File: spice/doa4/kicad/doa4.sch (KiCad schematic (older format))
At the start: 15 parts, among them Q1 BC557, Q2 BC557, Q3 BC547, Q4 BC547, Q5 BC557, Q6 BC547, Q7 BC547

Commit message: schema doa4 cont.
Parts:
- added D5, D6, D7, D8: D1418, ~, symbol DIODE
- added Q10: BC547, TO92, symbol BC547
- added Q11: BD139, TO126, symbol BD139
- added Q12: BD140, TO126, symbol BD140
- added Q8, Q9: BC557, TO92, symbol BC557
- added RCS2, RE1: 150, ~, symbol R
- added RE2, RE3: 10, ~, symbol R
- added RSZ3: 3800, ~, symbol R
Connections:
- net labels added: Odiff, Out, VrefCS
- wire segments 14 -> 37
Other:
- moved on the sheet: D1, D2, D3, D4, Q1, Q2, Q3, Q4, Q5, Q6, Q7, RCS1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

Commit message: schema doa4 cont.
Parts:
- added Cp1: 10p, ~, symbol C
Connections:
- wire segments 37 -> 38
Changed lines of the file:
@@
 Connection ~ 7150 3500
 Connection ~ 7750 3600
+$Comp
+L C Cp1
+U 1 1 592DCC26
+P 5750 4000
+F 0 "Cp1" H 5750 4100 40  0000 L CNN
+F 1 "10p" H 5756 3915 40  0000 L CNN
+F 2 "~" H 5788 3850 30  0000 C CNN
+F 3 "~" H 5750 4000 60  0000 C CNN
+	1    5750 4000
+	-1   0    0    1
+$EndComp
+Wire Wire Line
+	6000 3800 5750 3800
 $EndSCHEMATC

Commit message: doa4 cont
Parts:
- added C4, C5: 0.1u, ~, symbol C
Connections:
- net labels added: GND
- wire segments 38 -> 41
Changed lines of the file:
@@
 Sheet 1 1
 Title ""
-Date "30 may 2017"
+Date "2 jun 2017"
 Rev ""
 Comp ""
@@
 	4100 2100 4100 2000
 Wire Wire Line
-	4100 2000 7250 2000
+	4100 2000 8400 2000
 Text Label 4250 2000 0    60   ~ 0
 V+
@@
 Connection ~ 4350 3900
 Wire Wire Line
-	3800 4900 7250 4900
+	3800 4900 8400 4900
 Text Label 4300 4300 0    60   ~ 0
 V-
@@
 Wire Wire Line
 	6000 3800 5750 3800
+$Comp
+L C C4
+U 1 1 59318096
+P 8400 2200
+F 0 "C4" H 8400 2300 40  0000 L CNN
+F 1 "0.1u" H 8406 2115 40  0000 L CNN
+F 2 "~" H 8438 2050 30  0000 C CNN
+F 3 "~" H 8400 2200 60  0000 C CNN
+	1    8400 2200
+	1    0    0    -1
+$EndComp
+$Comp
+L C C5
+U 1 1 593180A3
+P 8400 4700
+F 0 "C5" H 8400 4800 40  0000 L CNN
+F 1 "0.1u" H 8406 4615 40  0000 L CNN
+F 2 "~" H 8438 4550 30  0000 C CNN
+F 3 "~" H 8400 4700 60  0000 C CNN
+	1    8400 4700
+	1    0    0    -1
+$EndComp
+Connection ~ 7250 2000
+Connection ~ 7250 4900
+Wire Wire Line
+	8400 4500 8400 2400
+$Comp
+L GND #PWR01
+U 1 1 593181CB
+P 8750 3550
+F 0 "#PWR01" H 8750 3550 30  0001 C CNN
+F 1 "GND" H 8750 3480 30  0001 C CNN
+F 2 "" H 8750 3550 60  0000 C CNN
+F 3 "" H 8750 3550 60  0000 C CNN
+	1    8750 3550
+	1    0    0    -1
+$EndComp
+Wire Wire Line
+	8750 3550 8750 3400
+Wire Wire Line
+	8750 3400 8400 3400
+Connection ~ 8400 3400
+$Comp
+L PWR_FLAG #FLG02
+U 1 1 5931836C
+P 8400 4150
+F 0 "#FLG02" H 8400 4245 30  0001 C CNN
+F 1 "PWR_FLAG" H 8400 4330 30  0000 C CNN
+F 2 "" H 8400 4150 60  0000 C CNN
+F 3 "" H 8400 4150 60  0000 C CNN
+	1    8400 4150
+	0    1    1    0
+$EndComp
+Connection ~ 8400 4150
 $EndSCHEMATC

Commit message: doa4 kicad 4.05
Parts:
- C4, C5, Cp1: footprint ~ -> Doa4FPLibrary:C_Rect_L4.6mm_W3.0mm_P2.50mm_MKS02_FKP02_Doa4; symbol C -> C-RESCUE-doa4
- D1: footprint ~ -> Diodes_THT:D_DO-41_SOD81_P2.54mm_Vertical_AnodeUp
- D2: footprint ~ -> Doa4FPLibrary:D_DO-41_SOD81_P2.54mm_Vertical_AnodeUp_Doa4
- D3: value D14148 -> D1N4148; footprint ~ -> Doa4FPLibrary:D_DO-41_SOD81_P2.54mm_Vertical_AnodeUp_Doa4
- D4: value D1418 -> D1N4148; footprint ~ -> Doa4FPLibrary:D_DO-41_SOD81_P2.54mm_Vertical_AnodeUp_Doa4
- D5, D6, D7, D8: value D1418 -> D1N4148; footprint ~ -> (none)
- Q1, Q10, Q2, Q3, Q4, Q5, Q6, Q7, Q8, Q9: footprint TO92 -> Doa4FPLibrary:TO-92_Molded_Wide_BCXXX
- Q11, Q12: footprint TO126 -> Doa4FPLibrary:TO-126_Vertical_Doa4
- RCS1, RCS2, RE1, RE2, RE3, RPCS1, RSZ1, RSZ2, RSZ3: footprint ~ -> Doa4FPLibrary:R_Axial_DIN0207_L6.3mm_D2.5mm_P2.54mm_Vertical_Doa4; symbol R -> R-RESCUE-doa4
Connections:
- net labels added: Emiter
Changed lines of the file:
@@
 EESchema Schematic File Version 2
+LIBS:doa4-rescue
 LIBS:power
 LIBS:device
@@
 LIBS:memory
 LIBS:xilinx
-LIBS:special
 LIBS:microcontrollers
 LIBS:dsp
@@
 LIBS:valves
 LIBS:doa4-cache
-EELAYER 27 0
+EELAYER 25 0
 EELAYER END
 $Descr A4 11693 8268
@@
 F 0 "Q5" H 4200 2651 40  0000 R CNN
 F 1 "BC557" H 4200 2950 40  0000 R CNN
-F 2 "TO92" H 4100 2902 29  0000 C CNN
+F 2 "Doa4FPLibrary:TO-92_Molded_Wide_BCXXX" H 4100 2902 29  0001 C CNN
 F 3 "" H 4200 2800 60  0000 C CNN
 	1    4200 2800
@@
 F 0 "Q1" H 3700 3051 40  0000 R CNN
 F 1 "BC557" H 3700 3350 40  0000 R CNN
-F 2 "TO92" H 3600 3302 29  0000 C CNN
+F 2 "Doa4FPLibrary:TO-92_Molded_Wide_BCXXX" H 3600 3302 29  0001 C CNN
 F 3 "" H 3700 3200 60  0000 C CNN
 	1    3700 3200
@@
 F 0 "Q2" H 4750 3051 40  0000 R CNN
 F 1 "BC557" H 4750 3350 40  0000 R CNN
-F 2 "TO92" H 4650 3302 29  0000 C CNN
+F 2 "Doa4FPLibrary:TO-92_Molded_Wide_BCXXX" H 4650 3302 29  0001 C CNN
 F 3 "" H 4750 3200 60  0000 C CNN
 	1    4750 3200
@@
 F 0 "Q3" H 4000 3251 40  0000 R CNN
 F 1 "BC547" H 4000 3550 40  0000 R CNN
-F 2 "TO92" H 3900 3502 29  0000 C CNN
+F 2 "Doa4FPLibrary:TO-92_Molded_Wide_BCXXX" H 3900 3502 29  0001 C CNN
 F 3 "" H 4000 3400 60  0000 C CNN
 	1    4000 3400
@@
 F 0 "Q4" H 4450 3251 40  0000 R CNN
 F 1 "BC547" H 4450 3550 40  0000 R CNN
-F 2 "TO92" H 4350 3502 29  0000 C CNN
+F 2 "Doa4FPLibrary:TO-92_Molded_Wide_BCXXX" H 4350 3502 29  0001 C CNN
 F 3 "" H 4450 3400 60  0000 C CNN
 	1    4450 3400
@@
 Connection ~ 4350 3000
 $Comp
-L R RCS1
+L R-RESCUE-doa4 RCS1
 U 1 1 592DBEC2
 P 4100 2350
 F 0 "RCS1" V 4180 2350 40  0000 C CNN
 F 1 "2700" V 4107 2351 40  0000 C CNN
-F 2 "~" V 4030 2350 30  0000 C CNN
+F 2 "Doa4FPLibrary:R_Axial_DIN0207_L6.3mm_D2.5mm_P2.54mm_Vertical_Doa4" V 4030 2350 30  0001 C CNN
 F 3 "~" H 4100 2350 30  0000 C CNN
 	1    4100 2350
@@
 P 4400 2600
 F 0 "D3" H 4400 2700 40  0000 C CNN
-F 1 "D14148" H 4400 2500 40  0000 C CNN
-F 2 "~" H 4400 2600 60  0000 C CNN
+F 1 "D1N4148" H 4400 2500 40  0000 C CNN
+F 2 "Doa4FPLibrary:D_DO-41_SOD81_P2.54mm_Vertical_AnodeUp_Doa4" H 4400 2600 60  0001 C CNN
 F 3 "~" H 4400 2600 60  0000 C CNN
 	1    4400 2600
@@
 P 4400 2200
 F 0 "D4" H 4400 2300 40  0000 C CNN
-F 1 "D1418" H 4400 2100 40  0000 C CNN
-F 2 "~" H 4400 2200 60  0000 C CNN
+F 1 "D1N4148" H 4400 2100 40  0000 C CNN
+F 2 "Doa4FPLibrary:D_DO-41_SOD81_P2.54mm_Vertical_AnodeUp_Doa4" H 4400 2200 60  0001 C CNN
 F 3 "~" H 4400 2200 60  0000 C CNN
 	1    4400 2200
@@
 Wire Wire Line
 	4100 2100 4100 2000
-Wire Wire Line
-	4100 2000 8400 2000
 Text Label 4250 2000 0    60   ~ 0
 V+
 $Comp
-L R RPCS1
+L R-RESCUE-doa4 RPCS1
 U 1 1 592DBF52
 P 4950 2800
 F 0 "RPCS1" V 5030 2800 40  0000 C CNN
 F 1 "27000" V 4957 2801 40  0000 C CNN
-F 2 "~" V 4880 2800 30  0000 C CNN
+F 2 "Doa4FPLibrary:R_Axial_DIN0207_L6.3mm_D2.5mm_P2.54mm_Vertical_Doa4" V 4880 2800 30  0001 C CNN
 F 3 "~" H 4950 2800 30  0000 C CNN
 	1    4950 2800
@@
 V-
 $Comp
-L R RSZ1
+L R-RESCUE-doa4 RSZ1
 U 1 1 592DBFEC
 P 3800 3650
 F 0 "RSZ1" V 3880 3650 40  0000 C CNN
 F 1 "3800" V 3807 3651 40  0000 C CNN
-F 2 "~" V 3730 3650 30  0000 C CNN
+F 2 "Doa4FPLibrary:R_Axial_DIN0207_L6.3mm_D2.5mm_P2.54mm_Vertical_Doa4" V 3730 3650 30  0001 C CNN
 F 3 "~" H 3800 3650 30  0000 C CNN
 	1    3800 3650
@@
 $EndComp
 $Comp
-L R RSZ2
+L R-RESCUE-doa4 RSZ2
 U 1 1 592DBFF8
 P 4650 3650
 F 0 "RSZ2" V 4730 3650 40  0000 C CNN
 F 1 "3800" V 4657 3651 40  0000 C CNN
-F 2 "~" V 4580 3650 30  0000 C CNN
+F 2 "Doa4FPLibrary:R_Axial_DIN0207_L6.3mm_D2.5mm_P2.54mm_Vertical_Doa4" V 4580 3650 30  0001 C CNN
 F 3 "~" H 4650 3650 30  0000 C CNN
 	1    4650 3650
@@
 F 0 "Q6" H 3900 4551 40  0000 R CNN
 F 1 "BC547" H 3900 4850 40  0000 R CNN
-F 2 "TO92" H 3800 4802 29  0000 C CNN
+F 2 "Doa4FPLibrary:TO-92_Molded_Wide_BCXXX" H 3800 4802 29  0001 C CNN
 F 3 "" H 3900 4700 60  0000 C CNN
 	1    3900 4700
@@
 F 0 "Q7" H 4550 4551 40  0000 R CNN
 F 1 "BC547" H 4550 4850 40  0000 R CNN
-F 2 "TO92" H 4450 4802 29  0000 C CNN
+F 2 "Doa4FPLibrary:TO-92_Molded_Wide_BCXXX" H 4450 4802 29  0001 C CNN
 F 3 "" H 4550 4700 60  0000 C CNN
 	1    4550 4700
@@
 F 0 "D1" H 3250 3500 40  0000 C CNN
 F 1 "D1N4148" H 3250 3300 40  0000 C CNN
-F 2 "~" H 3250 3400 60  0000 C CNN
+F 2 "Diodes_THT:D_DO-41_SOD81_P2.54mm_Vertical_AnodeUp" H 3250 3400 60  0001 C CNN
 F 3 "~" H 3250 3400 60  0000 C CNN
 	1    3250 3400
@@
 F 0 "D2" H 3400 3500 40  0000 C CNN
 F 1 "D1N4148" H 3400 3300 40  0000 C CNN
-F 2 "~" H 3400 3400 60  0000 C CNN
+F 2 "Doa4FPLibrary:D_DO-41_SOD81_P2.54mm_Vertical_AnodeUp_Doa4" H 3400 3400 60  0001 C CNN
 F 3 "~" H 3400 3400 60  0000 C CNN
 	1    3400 3400
@@
 VrefCS
 $Comp
-L R RCS2
+L R-RESCUE-doa4 RCS2
 U 1 1 592DC3EC
 P 6500 2350
 F 0 "RCS2" V 6580 2350 40  0000 C CNN
 F 1 "150" V 6507 2351 40  0000 C CNN
-F 2 "~" V 6430 2350 30  0000 C CNN
+F 2 "Doa4FPLibrary:R_Axial_DIN0207_L6.3mm_D2.5mm_P2.54mm_Vertical_Doa4" V 6430 2350 30  0001 C CNN
 F 3 "~" H 6500 2350 30  0000 C CNN
 	1    6500 2350
@@
 F 0 "Q8" H 6400 2651 40  0000 R CNN
 F 1 "BC557" H 6400 2950 40  0000 R CNN
-F 2 "TO92" H 6300 2902 29  0000 C CNN
+F 2 "Doa4FPLibrary:TO-92_Molded_Wide_BCXXX" H 6300 2902 29  0001 C CNN
 F 3 "" H 6400 2800 60  0000 C CNN
 	1    6400 2800
@@
 P 6500 3200
 F 0 "D5" H 6500 3300 40  0000 C CNN
-F 1 "D1418" H 6500 3100 40  0000 C CNN
-F 2 "~" H 6500 3200 60  0000 C CNN
+F 1 "D1N4148" H 6500 3100 40  0000 C CNN
+F 2 "" H 6500 3200 60  0000 C CNN
 F 3 "~" H 6500 3200 60  0000 C CNN
 	1    6500 3200
@@
 P 6500 3600
 F 0 "D6" H 6500 3700 40  0000 C CNN
-F 1 "D1418" H 6500 3500 40  0000 C CNN
-F 2 "~" H 6500 3600 60  0000 C CNN
+F 1 "D1N4148" H 6500 3500 40  0000 C CNN
+F 2 "" H 6500 3600 60  0000 C CNN
 F 3 "~" H 6500 3600 60  0000 C CNN
 	1    6500 3600
@@
 F 0 "Q9" H 6400 3851 40  0000 R CNN
 F 1 "BC557" H 6400 4150 40  0000 R CNN
-F 2 "TO92" H 6300 4102 29  0000 C CNN
+F 2 "Doa4FPLibrary:TO-92_Molded_Wide_BCXXX" H 6300 4102 29  0001 C CNN
 F 3 "" H 6400 4000 60  0000 C CNN
 	1    6400 4000
@@
 F 0 "Q10" H 6100 4051 40  0000 R CNN
 F 1 "BC547" H 6100 4350 40  0000 R CNN
-F 2 "TO92" H 6000 4302 29  0000 C CNN
+F 2 "Doa4FPLibrary:TO-92_Molded_Wide_BCXXX" H 6000 4302 29  0001 C CNN
 F 3 "" H 6100 4200 60  0000 C CNN
 	1    6100 4200
@@
 	6500 4400 6200 4400
 $Comp
-L R RSZ3
+L R-RESCUE-doa4 RSZ3
 U 1 1 592DC668
 P 6250 3800
 F 0 "RSZ3" V 6330 3800 40  0000 C CNN
 F 1 "3800" V 6257 3801 40  0000 C CNN
-F 2 "~" V 6180 3800 30  0000 C CNN
+F 2 "Doa4FPLibrary:R_Axial_DIN0207_L6.3mm_D2.5mm_P2.54mm_Vertical_Doa4" V 6180 3800 30  0001 C CNN
 F 3 "~" H 6250 3800 30  0000 C CNN
 	1    6250 3800
@@
 	6000 4000 6000 3800
 $Comp
-L R RE1
+L R-RESCUE-doa4 RE1
 U 1 1 592DC702
 P 6500 4650
 F 0 "RE1" V 6580 4650 40  0000 C CNN
 F 1 "150" V 6507 4651 40  0000 C CNN
-F 2 "~" V 6430 4650 30  0000 C CNN
+F 2 "Doa4FPLibrary:R_Axial_DIN0207_L6.3mm_D2.5mm_P2.54mm_Vertical_Doa4" V 6430 4650 30  0001 C CNN
 F 3 "~" H 6500 4650 30  0000 C CNN
 	1    6500 4650
@@
 F 0 "Q11" H 7150 2850 40  0000 R CNN
 F 1 "BD139" H 7150 3150 40  0000 R CNN
-F 2 "TO126" H 7030 3100 29  0001 C CNN
+F 2 "Doa4FPLibrary:TO-126_Vertical_Doa4" H 7030 3100 29  0001 C CNN
 F 3 "" H 7150 3000 60  0000 C CNN
 	1    7150 3000
@@
 F 0 "Q12" H 7150 3650 40  0000 R CNN
 F 1 "BD140" H 7150 3950 40  0000 R CNN
-F 2 "TO126" H 7030 3900 29  0001 C CNN
+F 2 "Doa4FPLibrary:TO-126_Vertical_Doa4" H 7030 3900 29  0001 C CNN
 F 3 "" H 7150 3800 60  0000 C CNN
 	1    7150 3800
-	1    0    0    -1
-$EndComp
-$Comp
-L R RE2
+	1    0    0    1
+$EndComp
+$Comp
+L R-RESCUE-doa4 RE2
 U 1 1 592DCB70
 P 7500 3200
 F 0 "RE2" V 7580 3200 40  0000 C CNN
 F 1 "10" V 7507 3201 40  0000 C CNN
-F 2 "~" V 7430 3200 30  0000 C CNN
+F 2 "Doa4FPLibrary:R_Axial_DIN0207_L6.3mm_D2.5mm_P2.54mm_Vertical_Doa4" V 7430 3200 30  0001 C CNN
 F 3 "~" H 7500 3200 30  0000 C CNN
 	1    7500 3200
@@
 $EndComp
 $Comp
-L R RE3
+L R-RESCUE-doa4 RE3
 U 1 1 592DCB9D
 P 7500 3600
 F 0 "RE3" V 7580 3600 40  0000 C CNN
 F 1 "10" V 7507 3601 40  0000 C CNN
-F 2 "~" V 7430 3600 30  0000 C CNN
+F 2 "Doa4FPLibrary:R_Axial_DIN0207_L6.3mm_D2.5mm_P2.54mm_Vertical_Doa4" V 7430 3600 30  0001 C CNN
 F 3 "~" H 7500 3600 30  0000 C CNN
 	1    7500 3600
@@
 P 6950 3300
 F 0 "D7" H 6950 3400 40  0000 C CNN
-F 1 "D1418" H 6950 3200 40  0000 C CNN
-F 2 "~" H 6950 3300 60  0000 C CNN
+F 1 "D1N4148" H 6950 3200 40  0000 C CNN
+F 2 "" H 6950 3300 60  0000 C CNN
 F 3 "~" H 6950 3300 60  0000 C CNN
 	1    6950 3300
@@
 P 6950 3500
 F 0 "D8" H 6950 3600 40  0000 C CNN
-F 1 "D1418" H 6950 3400 40  0000 C CNN
-F 2 "~" H 6950 3500 60  0000 C CNN
+F 1 "D1N4148" H 6950 3400 40  0000 C CNN
+F 2 "" H 6950 3500 60  0000 C CNN
 F 3 "~" H 6950 3500 60  0000 C CNN
 	1    6950 3500
@@
 Connection ~ 7750 3600
 $Comp
-L C Cp1
+L C-RESCUE-doa4 Cp1
 U 1 1 592DCC26
 P 5750 4000
 F 0 "Cp1" H 5750 4100 40  0000 L CNN
 F 1 "10p" H 5756 3915 40  0000 L CNN
-F 2 "~" H 5788 3850 30  0000 C CNN
+F 2 "Doa4FPLibrary:C_Rect_L4.6mm_W3.0mm_P2.50mm_MKS02_FKP02_Doa4" H 5788 3850 30  0001 C CNN
 F 3 "~" H 5750 4000 60  0000 C CNN
 	1    5750 4000
@@
 	6000 3800 5750 3800
 $Comp
-L C C4
+L C-RESCUE-doa4 C4
 U 1 1 59318096
 P 8400 2200
 F 0 "C4" H 8400 2300 40  0000 L CNN
 F 1 "0.1u" H 8406 2115 40  0000 L CNN
-F 2 "~" H 8438 2050 30  0000 C CNN
+F 2 "Doa4FPLibrary:C_Rect_L4.6mm_W3.0mm_P2.50mm_MKS02_FKP02_Doa4" H 8438 2050 30  0001 C CNN
 F 3 "~" H 8400 2200 60  0000 C CNN
 	1    8400 2200
@@
 $EndComp
 $Comp
-L C C5
+L C-RESCUE-doa4 C5
 U 1 1 593180A3
 P 8400 4700
 F 0 "C5" H 8400 4800 40  0000 L CNN
 F 1 "0.1u" H 8406 4615 40  0000 L CNN
-F 2 "~" H 8438 4550 30  0000 C CNN
+F 2 "Doa4FPLibrary:C_Rect_L4.6mm_W3.0mm_P2.50mm_MKS02_FKP02_Doa4" H 8438 4550 30  0000 C CNN
 F 3 "~" H 8400 4700 60  0000 C CNN
 	1    8400 4700
@@
 	8400 4500 8400 2400
 $Comp
-L GND #PWR01
+L GND-RESCUE-doa4 #PWR01
 U 1 1 593181CB
 P 8750 3550
@@
 $EndComp
 Connection ~ 8400 4150
+Wire Wire Line
+	4100 2000 8400 2000
+Text Label 3850 3000 0    60   ~ 0
+Emiter
+Entry Wire Line
+	8450 2250 8550 2350
 $EndSCHEMATC

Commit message: init location input
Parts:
- D5, D6, D7, D8: footprint (none) -> Doa4FPLibrary:D_DO-41_SOD81_P2.54mm_Vertical_AnodeUp_Doa4
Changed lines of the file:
@@
 F 0 "D5" H 6500 3300 40  0000 C CNN
 F 1 "D1N4148" H 6500 3100 40  0000 C CNN
-F 2 "" H 6500 3200 60  0000 C CNN
+F 2 "Doa4FPLibrary:D_DO-41_SOD81_P2.54mm_Vertical_AnodeUp_Doa4" H 6500 3200 60  0001 C CNN
 F 3 "~" H 6500 3200 60  0000 C CNN
 	1    6500 3200
@@
 F 0 "D6" H 6500 3700 40  0000 C CNN
 F 1 "D1N4148" H 6500 3500 40  0000 C CNN
-F 2 "" H 6500 3600 60  0000 C CNN
+F 2 "Doa4FPLibrary:D_DO-41_SOD81_P2.54mm_Vertical_AnodeUp_Doa4" H 6500 3600 60  0001 C CNN
 F 3 "~" H 6500 3600 60  0000 C CNN
 	1    6500 3600
@@
 F 0 "D7" H 6950 3400 40  0000 C CNN
 F 1 "D1N4148" H 6950 3200 40  0000 C CNN
-F 2 "" H 6950 3300 60  0000 C CNN
+F 2 "Doa4FPLibrary:D_DO-41_SOD81_P2.54mm_Vertical_AnodeUp_Doa4" H 6950 3300 60  0001 C CNN
 F 3 "~" H 6950 3300 60  0000 C CNN
 	1    6950 3300
@@
 F 0 "D8" H 6950 3600 40  0000 C CNN
 F 1 "D1N4148" H 6950 3400 40  0000 C CNN
-F 2 "" H 6950 3500 60  0000 C CNN
+F 2 "Doa4FPLibrary:D_DO-41_SOD81_P2.54mm_Vertical_AnodeUp_Doa4" H 6950 3500 60  0001 C CNN
 F 3 "~" H 6950 3500 60  0000 C CNN
 	1    6950 3500

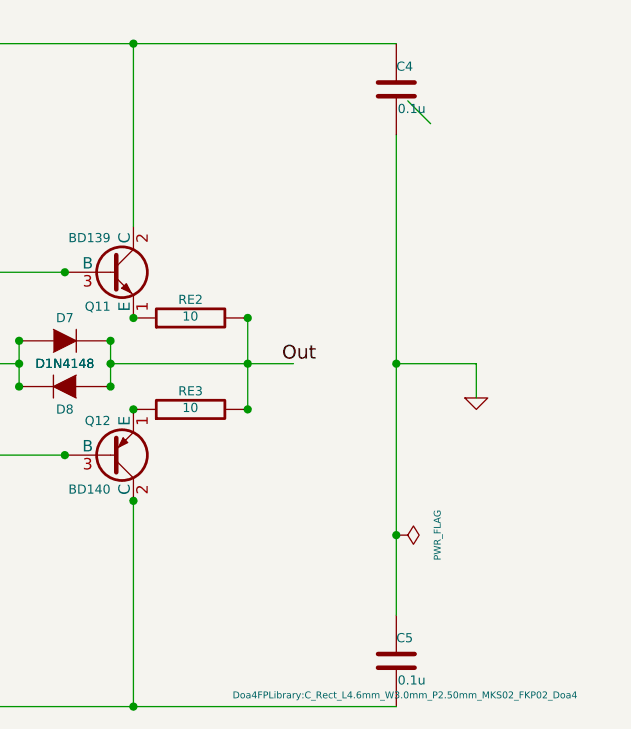
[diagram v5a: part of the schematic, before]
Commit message: conn j990 added
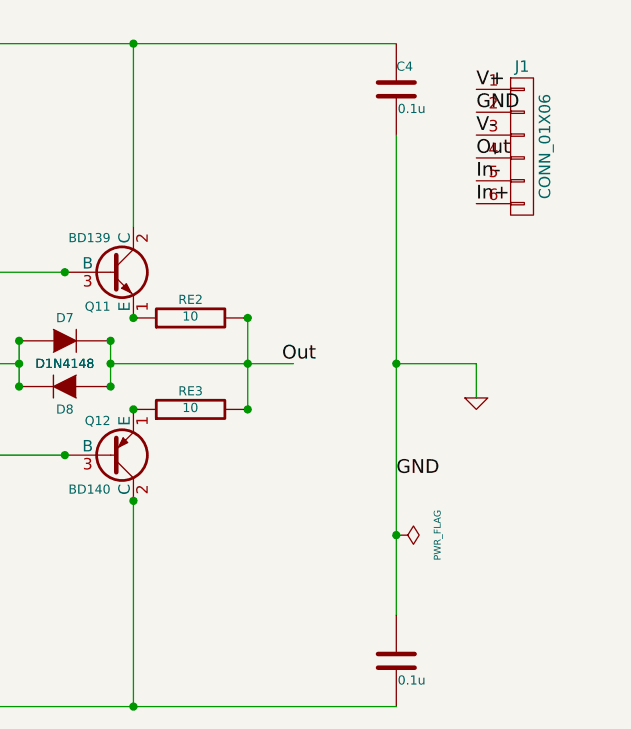
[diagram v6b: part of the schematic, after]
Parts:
- added J1: CONN_01X06, Doa4FPLibrary:j990, symbol CONN_01X06
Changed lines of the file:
@@
 U 1 1 593180A3
 P 8400 4700
-F 0 "C5" H 8400 4800 40  0000 L CNN
+F 0 "C5" H 8400 4800 40  0001 L CNN
 F 1 "0.1u" H 8406 4615 40  0000 L CNN
-F 2 "Doa4FPLibrary:C_Rect_L4.6mm_W3.0mm_P2.50mm_MKS02_FKP02_Doa4" H 8438 4550 30  0000 C CNN
+F 2 "Doa4FPLibrary:C_Rect_L4.6mm_W3.0mm_P2.50mm_MKS02_FKP02_Doa4" H 8438 4550 30  0001 C CNN
 F 3 "~" H 8400 4700 60  0000 C CNN
 	1    8400 4700
@@
 Text Label 3850 3000 0    60   ~ 0
 Emiter
-Entry Wire Line
-	8450 2250 8550 2350
+$Comp
+L CONN_01X06 J1
+U 1 1 5936F09F
+P 8950 2450
+F 0 "J1" H 8950 2800 50  0000 C CNN
+F 1 "CONN_01X06" V 9050 2450 50  0000 C CNN
+F 2 "Doa4FPLibrary:j990" H 8950 2450 50  0001 C CNN
+F 3 "" H 8950 2450 50  0001 C CNN
+	1    8950 2450
+	1    0    0    -1
+$EndComp
+Text Label 8750 2200 0    60   ~ 0
+V+
+Text Label 8400 3900 0    60   ~ 0
+GND
+Text Label 8750 2300 0    60   ~ 0
+GND
+Text Label 8750 2400 0    60   ~ 0
+V-
+Text Label 8750 2500 0    60   ~ 0
+Out
+Text Label 8750 2600 0    60   ~ 0
+In-
+Text Label 8750 2700 0    60   ~ 0
+In+
 $EndSCHEMATC

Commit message: location init
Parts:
- added RCP1: 380, Doa4FPLibrary:R_Axial_DIN0207_L6.3mm_D2.5mm_P2.54mm_Vertical_Doa4, symbol R-RESCUE-doa4
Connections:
- wire segments 41 -> 61
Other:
- moved on the sheet: Cp1
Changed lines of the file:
@@
 $EndComp
 Wire Wire Line
-	3800 3000 4650 3000
+	3800 3000 4100 3000
+Wire Wire Line
+	4100 3000 4350 3000
+Wire Wire Line
+	4350 3000 4650 3000
 Wire Wire Line
 	4100 3000 4100 3200
@@
 $EndComp
 Wire Wire Line
-	4350 3600 4350 4700
+	4350 3600 4350 3900
+Wire Wire Line
+	4350 3900 4350 4700
 Wire Wire Line
 	4350 3900 4650 3900
@@
 Connection ~ 4350 3900
 Wire Wire Line
-	3800 4900 8400 4900
+	3800 4900 4650 4900
+Wire Wire Line
+	4650 4900 5350 4900
+Wire Wire Line
+	5350 4900 6500 4900
+Wire Wire Line
+	6500 4900 7250 4900
+Wire Wire Line
+	7250 4900 8400 4900
 Text Label 4300 4300 0    60   ~ 0
 V-
 Wire Wire Line
-	3150 3200 3500 3200
+	3150 3200 3250 3200
+Wire Wire Line
+	3250 3200 3400 3200
+Wire Wire Line
+	3400 3200 3500 3200
 Wire Wire Line
 	4950 3200 5250 3200
@@
 $EndComp
 Wire Wire Line
-	3100 3600 3400 3600
+	3100 3600 3250 3600
+Wire Wire Line
+	3250 3600 3400 3600
 Connection ~ 3250 3600
 Text Label 3150 3600 0    60   ~ 0
@@
 Connection ~ 4950 3200
 Wire Wire Line
-	4400 2800 4700 2800
+	4400 2800 4550 2800
+Wire Wire Line
+	4550 2800 4700 2800
 Connection ~ 4700 2800
 Text Label 4450 2800 0    60   ~ 0
@@
 $EndComp
 Wire Wire Line
-	5900 4200 5650 4200
+	5900 4200 5400 4200
 Text Label 5750 4200 0    60   ~ 0
 Odiff
@@
 	6950 3800 6500 3800
 Wire Wire Line
-	7750 3200 7750 3600
+	7750 3200 7750 3400
+Wire Wire Line
+	7750 3400 7750 3600
 Wire Wire Line
 	7250 2000 7250 2800
@@
 Connection ~ 7250 4000
 Wire Wire Line
-	7150 3400 7950 3400
+	7150 3400 7750 3400
+Wire Wire Line
+	7750 3400 7950 3400
 Connection ~ 7750 3400
 Text Label 7900 3400 0    60   ~ 0
@@
 $EndComp
 Wire Wire Line
-	7150 3300 7150 3500
+	7150 3300 7150 3400
+Wire Wire Line
+	7150 3400 7150 3500
 Connection ~ 7150 3400
 Wire Wire Line
-	6750 3300 6750 3500
+	6750 3300 6750 3400
+Wire Wire Line
+	6750 3400 6750 3500
 Wire Wire Line
 	6750 3400 6500 3400
@@
 L C-RESCUE-doa4 Cp1
 U 1 1 592DCC26
-P 5750 4000
-F 0 "Cp1" H 5750 4100 40  0000 L CNN
-F 1 "10p" H 5756 3915 40  0000 L CNN
-F 2 "Doa4FPLibrary:C_Rect_L4.6mm_W3.0mm_P2.50mm_MKS02_FKP02_Doa4" H 5788 3850 30  0001 C CNN
-F 3 "~" H 5750 4000 60  0000 C CNN
-	1    5750 4000
+P 5500 4000
+F 0 "Cp1" H 5500 4100 40  0000 L CNN
+F 1 "10p" H 5506 3915 40  0000 L CNN
+F 2 "Doa4FPLibrary:C_Rect_L4.6mm_W3.0mm_P2.50mm_MKS02_FKP02_Doa4" H 5538 3850 30  0001 C CNN
+F 3 "~" H 5500 4000 60  0000 C CNN
+	1    5500 4000
 	-1   0    0    1
 $EndComp
 Wire Wire Line
-	6000 3800 5750 3800
+	6000 3800 5950 3800
 $Comp
 L C-RESCUE-doa4 C4
@@
 Connection ~ 7250 4900
 Wire Wire Line
-	8400 4500 8400 2400
+	8400 4500 8400 4150
+Wire Wire Line
+	8400 4150 8400 3400
+Wire Wire Line
+	8400 3400 8400 2400
 $Comp
 L GND-RESCUE-doa4 #PWR01
@@
 Connection ~ 8400 4150
 Wire Wire Line
-	4100 2000 8400 2000
+	4100 2000 4400 2000
+Wire Wire Line
+	4400 2000 6500 2000
+Wire Wire Line
+	6500 2000 7250 2000
+Wire Wire Line
+	7250 2000 8400 2000
 Text Label 3850 3000 0    60   ~ 0
 Emiter
@@
 Text Label 8750 2700 0    60   ~ 0
 In+
+$Comp
+L R-RESCUE-doa4 RCP1
+U 1 1 5938275E
+P 5750 3800
+F 0 "RCP1" V 5830 3800 40  0000 C CNN
+F 1 "380" V 5757 3801 40  0000 C CNN
+F 2 "Doa4FPLibrary:R_Axial_DIN0207_L6.3mm_D2.5mm_P2.54mm_Vertical_Doa4" V 5680 3800 30  0001 C CNN
+F 3 "~" H 5750 3800 30  0000 C CNN
+	1    5750 3800
+	0    -1   -1   0
+$EndComp
+Connection ~ 5950 3800
 $EndSCHEMATC
